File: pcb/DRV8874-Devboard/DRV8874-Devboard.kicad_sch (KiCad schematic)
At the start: 21 parts, among them J1 Conn_01x04_Pin, J2 Screw_Terminal_01x02, J4 Conn_01x03_Pin, J5 Conn_01x04_Pin, J6 Conn_01x03_Pin, J7 Conn_01x03_Pin, J8 Conn_01x04_Pin, U1 DRV8874, U2 TinyThinker_J1, U3 TinyThinker_J2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

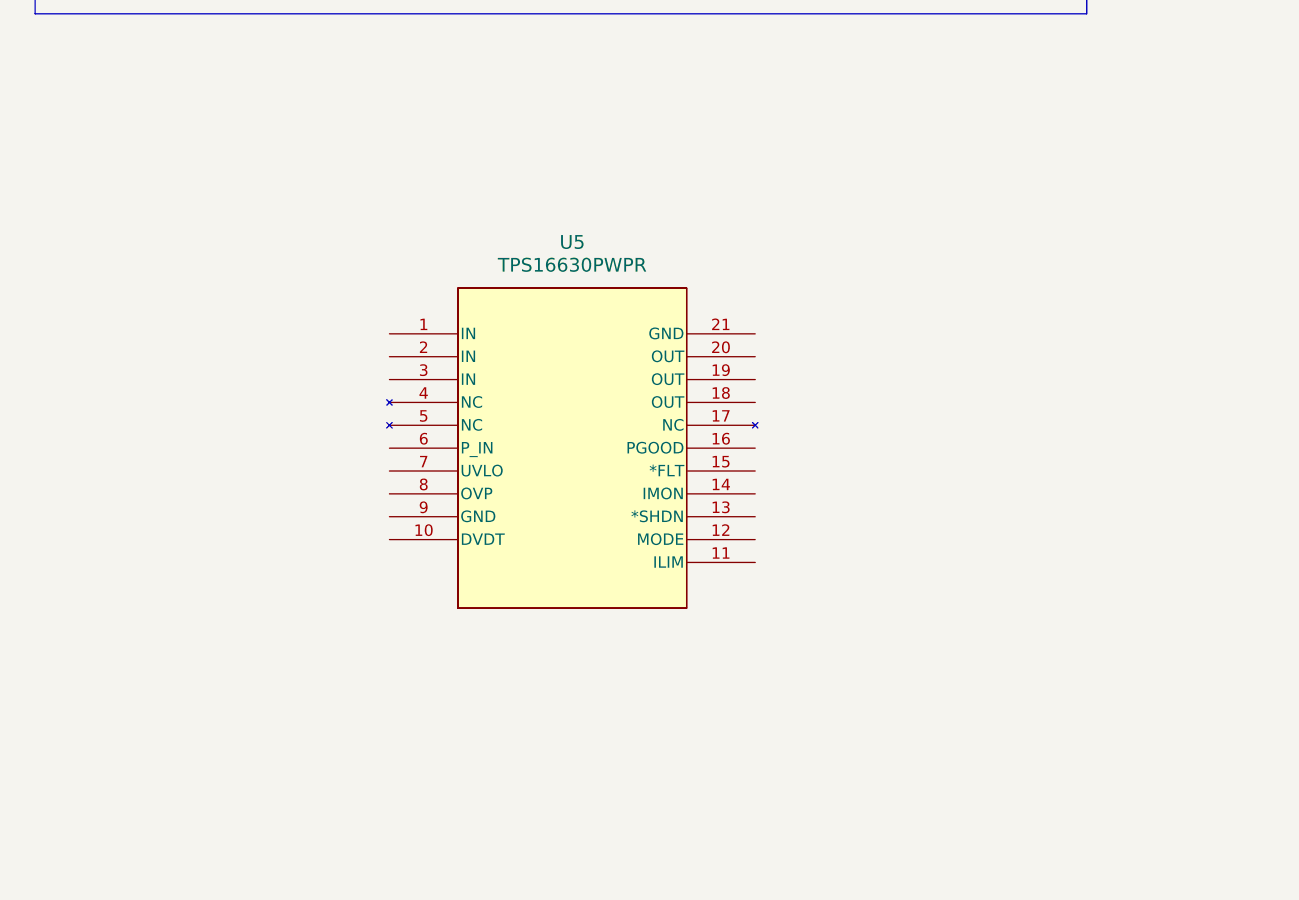
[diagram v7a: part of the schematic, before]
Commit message: started working on TPS16630
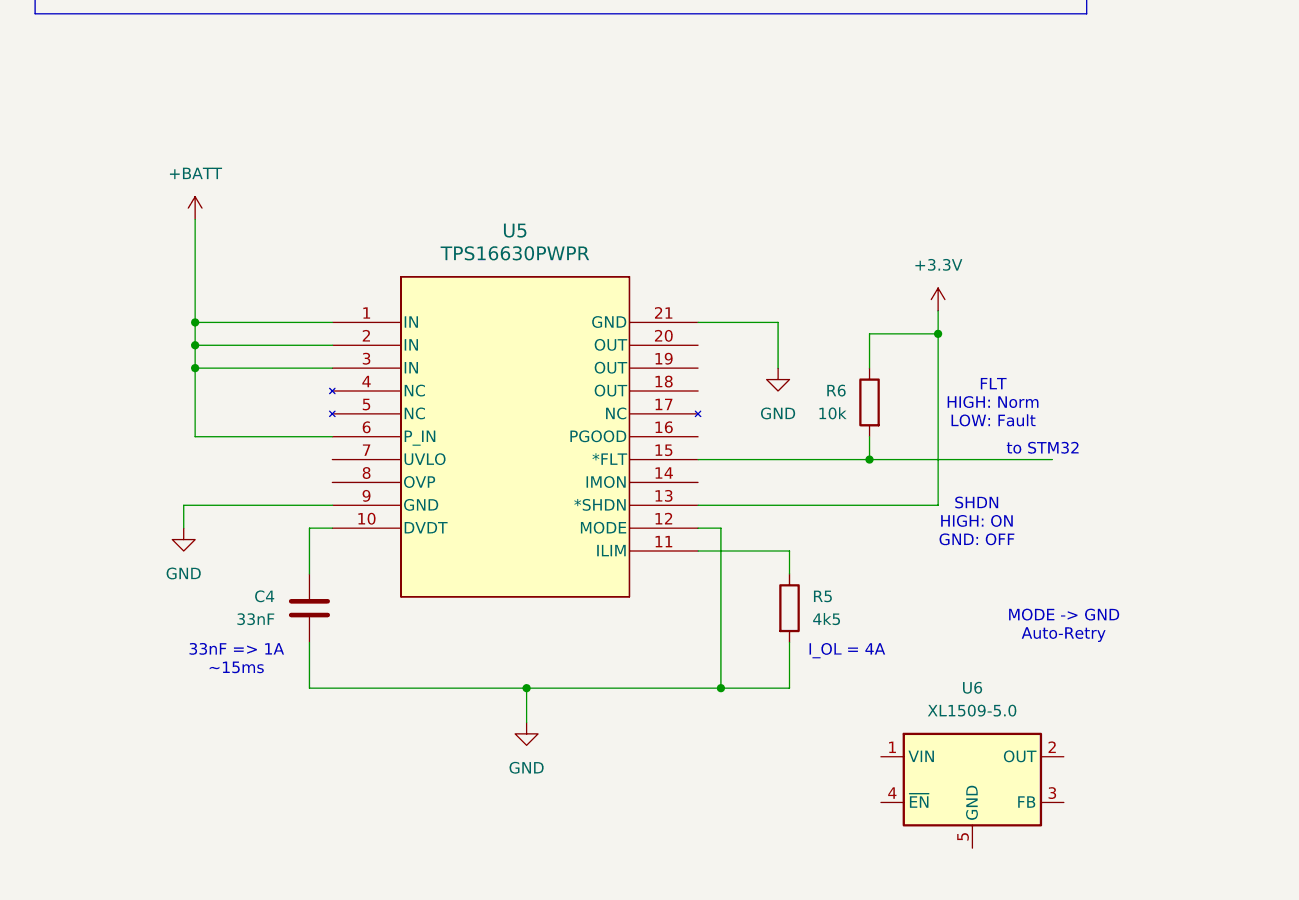
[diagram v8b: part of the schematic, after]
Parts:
- added C4: 33nF, Capacitor_SMD:C_0603_1608Metric, symbol Device:C
- added R5: 4k5, symbol Device:R
- added R6: 10k, symbol Device:R
- added U6: XL1509-5.0, Package_SO:SOIC-8_3.9x4.9mm_P1.27mm, symbol Regulator_Switching:XL1509-5.0
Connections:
- net +3.3V: now also U5.13 (*SHDN), R6.1
- net +BATT: now also U5.1 (IN), U5.2 (IN), U5.3 (IN), U5.6 (P_IN)
- net GND: now also U5.12 (MODE), U5.21 (GND), U5.9 (GND), C4.2, R5.2
- net at U5.10 (DVDT): now also C4.1
- net at U5.11 (ILIM): now also R5.1
- net at U5.15 (*FLT): now also R6.2
- new net: U6.5 (GND), U6.6 (GND), U6.7 (GND), U6.8 (GND)
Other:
- note added: "33nF => 1A ~15ms"
- note added: "FLT HIGH: Norm LOW: Fault"
- note added: "I_OL = 4A"
- note added: "MODE -> GND Auto-Retry"
- note added: "SHDN HIGH: ON GND: OFF"
- note added: "to STM32"
- moved on the sheet: U5
